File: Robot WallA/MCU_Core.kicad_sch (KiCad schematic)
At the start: 4 parts, among them IC2 STM32F407IGT6, Y1 Crystal_GND24

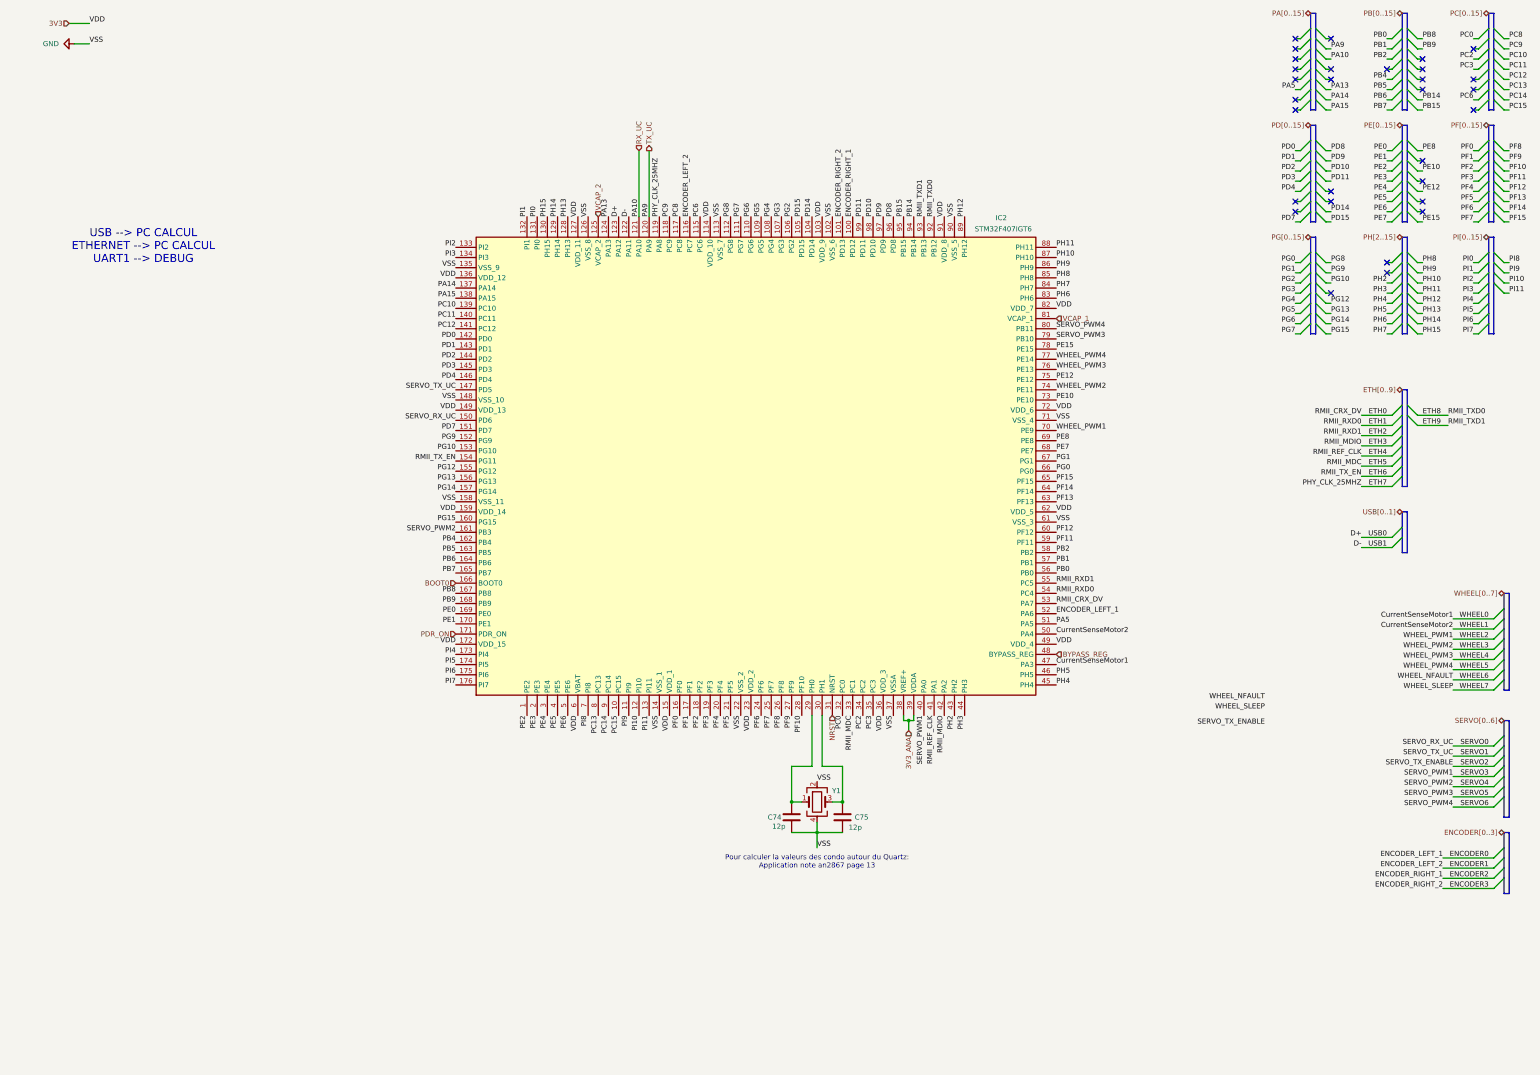
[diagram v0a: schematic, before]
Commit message: Continued to link MCU pins, Added a sheet for servomotors and optional 2 DC motors.
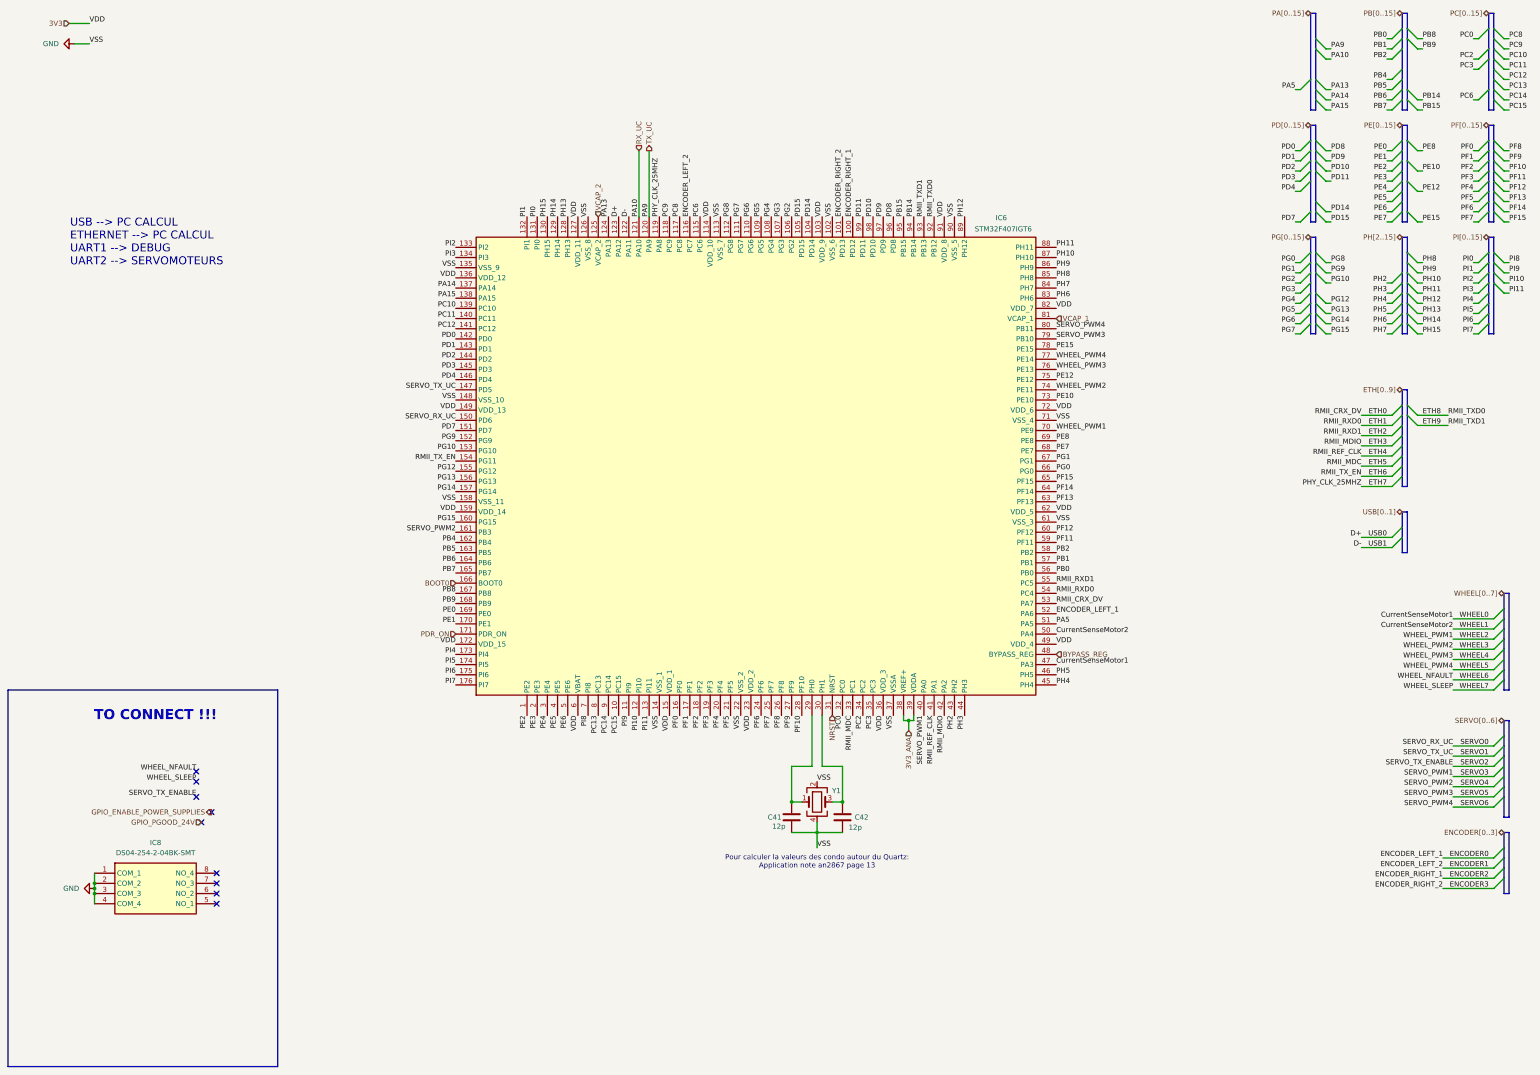
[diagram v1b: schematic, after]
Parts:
- added IC8: DS04-254-2-04BK-SMT, SOP254P990X430-8N, symbol SamacSys_new:DS04-254-2-04BK-SMT
- renumbered C74 to C41, C75 to C42, IC2 to IC6
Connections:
- net GND: now also IC8.1 (COM_1), IC8.2 (COM_2), IC8.3 (COM_3), IC8.4 (COM_4)
- no-connect marks 30 -> 9
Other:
- note added: "TO CONNECT !!!"
- note added: "USB --> PC CALCUL ETHERNET --> PC CALCUL UART1 --> DEBUG UART2 --> SERVOMOTEURS"
- note removed: "USB --> PC CALCUL ETHERNET --> PC CALCUL UART1 --> DEBUG"

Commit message: Defined every footprints
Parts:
- added J1: NC-Conn_02x05_Female, Connector_PinHeader_1.27mm:PinHeader_2x05_P1.27mm_Vertical, symbol SamacSys_Parts:Conn_02x05_Female
- C1: renamed from C41; value 12p -> 12pF; Manufacturer_Part_Number (none) -> C0603C120F5GACTU
- C2: renamed from C42; value 12p -> 12pF; Manufacturer_Part_Number (none) -> C0603C120F5GACTU
- IC1: renamed from IC6; footprint QFP50P2600X2600X160-176N -> SamacSys_Parts:QFP50P2600X2600X160-176N; Arrow Part Number STM32F407IGT6 -> (none); Arrow Price/Stock https://www.arrow.com/en/products/stm32f407igt6/stmicroelec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 -> (none); Height 1.6 -> (none); Manufacturer_Name STMicroelectronics -> (none); Mouser Part Number 511-STM32F407IGT6 -> (none); Mouser Price/Stock https://www.mouser.co.uk/ProductDetail/STMicroelectronics/S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 -> (none)
- IC2: renamed from IC8; footprint SOP254P990X430-8N -> SamacSys_Parts:SOP254P990X430-8N; Arrow Part Number DS04-254-2-04BK-SMT -> (none); Arrow Price/Stock https://www.arrow.com/en/products/ds04-254-2-04bk-smt/cui-d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 -> (none); Height 4.3 -> (none); Manufacturer_Name Same Sky -> (none); Mouser Part Number 490-DS04254204BK-SMT -> (none); Mouser Price/Stock https://www.mouser.co.uk/ProductDetail/Same-Sky/DS04-254-2-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 -> (none)
- Y1: footprint (none) -> Crystal:Crystal_SMD_3225-4Pin_3.2x2.5mm
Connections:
- net PC6 is gone; now on net ENCODER0: IC1.115 (PC6)
- net 3V3: now also J1.1
- net ENCODER0: no longer IC1.52 (PA6)
- net GND: now also J1.3, J1.5
- net NRST: now also J1.10
- net PA13 renamed SWDIO
- net SWDIO: now also J1.2
- net PA14 renamed SWCLK
- net SWCLK: now also J1.4
- net PB0 renamed SECONDARY_MOTOR1
- net PH10 renamed SECONDARY_MOTOR6
- net PH11 renamed SECONDARY_MOTOR7
- new net SECONDARY_MOTOR0: IC1.52 (PA6)
- no-connect marks 9 -> 17

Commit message: Updated USB UART converter, Linked telemeter sensors.
Updated components indicators
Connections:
- net PB4 is gone; now on net ENCODER0: IC1.162 (PB4)
- net PB5 is gone; now on net ENCODER1: IC1.163 (PB5)
- net ENCODER0: no longer IC1.115 (PC6)
- net ENCODER1: no longer IC1.116 (PC7)
- net PB1 renamed SENSORS0
- net PC0 renamed SENSORS1
- net PC2 renamed SENSORS2
- net PC3 renamed SENSORS3
- net PC8 renamed SENSORS9
- net PC9 renamed SENSORS8
- new net SENSORS10: IC1.116 (PC7)
- new net SENSORS11: IC1.115 (PC6)
- no-connect marks 17 -> 4

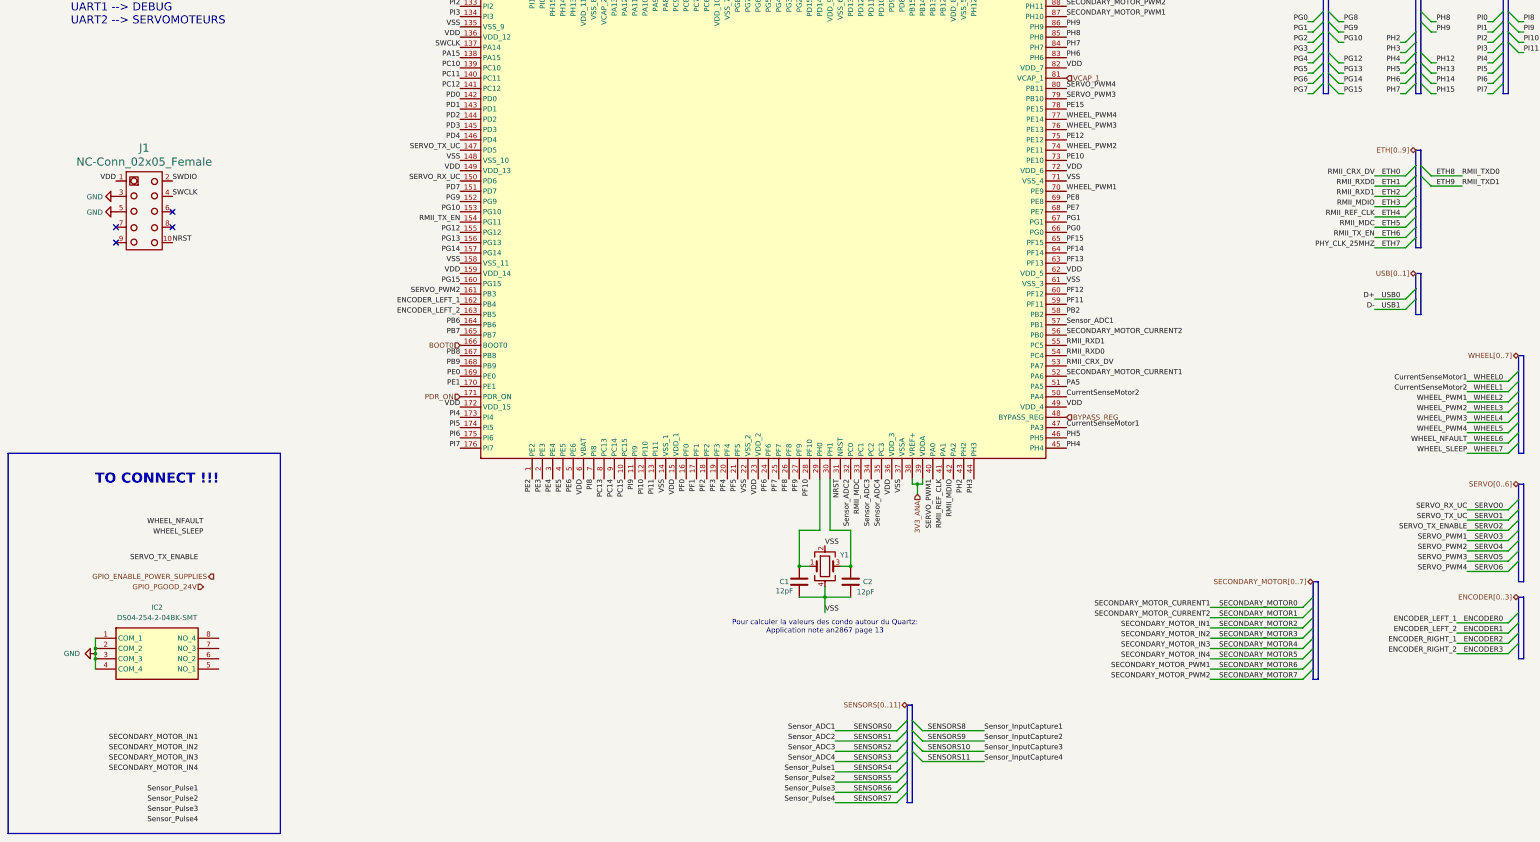
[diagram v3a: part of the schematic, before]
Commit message: Added standard switchs, debug leds and 12V and 5V connectors
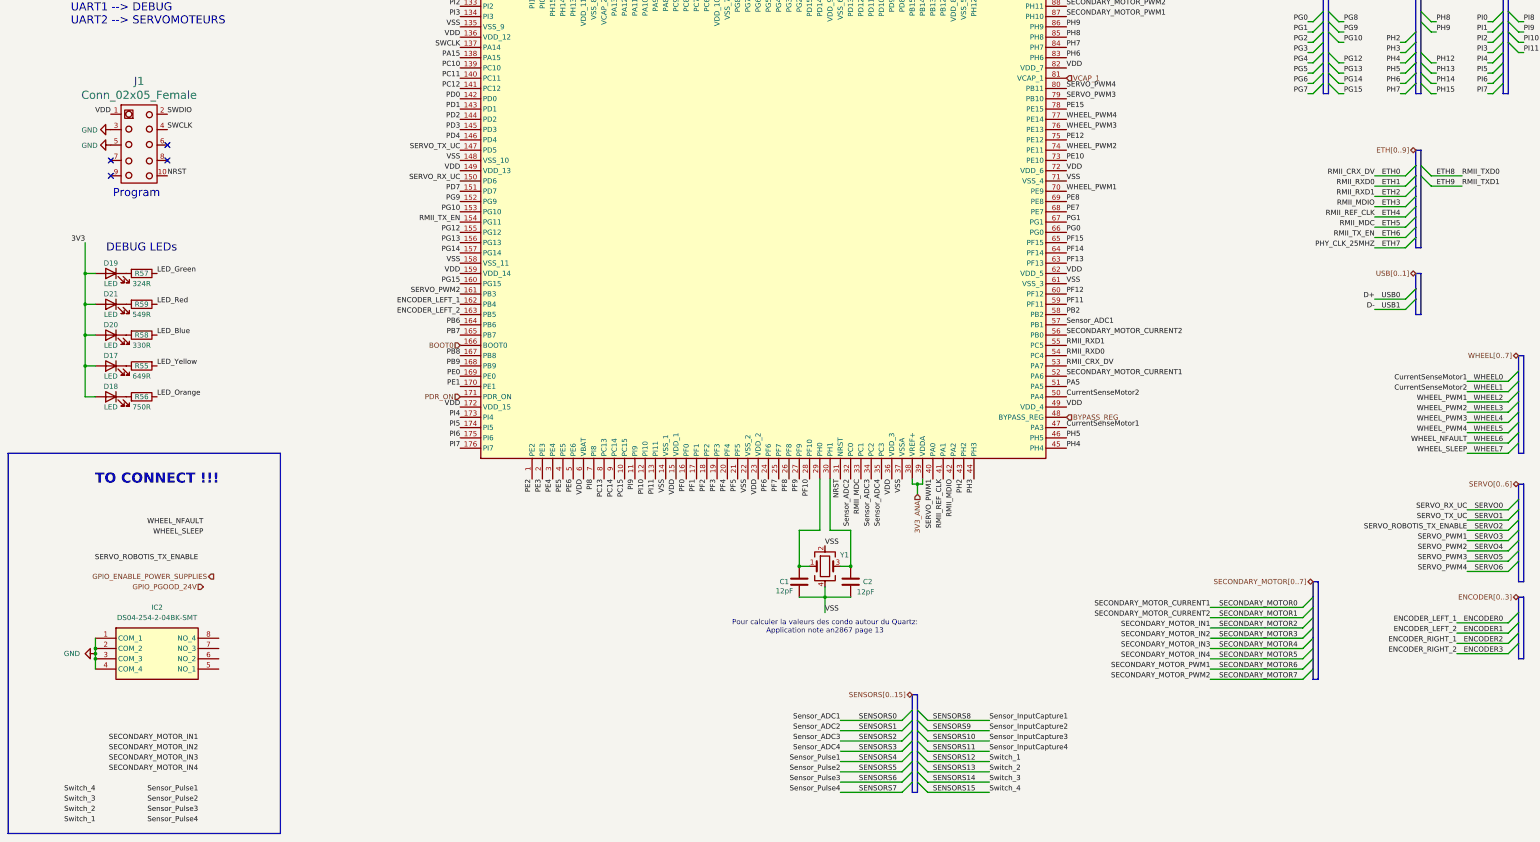
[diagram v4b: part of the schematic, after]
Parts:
- added D17, D18, D19, D20, D21: LED, LED_SMD:LED_0603_1608Metric, symbol Device:LED
- added R55: 649R, Resistor_SMD:R_0603_1608Metric, symbol Device:R
- added R56: 750R, Resistor_SMD:R_0603_1608Metric, symbol Device:R
- added R57: 324R, Resistor_SMD:R_0603_1608Metric, symbol Device:R
- added R58: 330R, Resistor_SMD:R_0603_1608Metric, symbol Device:R
- added R59: 549R, Resistor_SMD:R_0603_1608Metric, symbol Device:R
- J1: value NC-Conn_02x05_Female -> Conn_02x05_Female
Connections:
- net 3V3: now also D17.2 (A), D18.2 (A), D19.2 (A), D20.2 (A), D21.2 (A)
- new net: D17.1 (K), R55.1
- new net: D20.1 (K), R58.2
- new net: D18.1 (K), R56.2
- new net: D21.1 (K), R59.2
- new net: D19.1 (K), R57.2
- new net LED_Blue: R58.1
- new net LED_Green: R57.1
- new net LED_Orange: R56.1
- new net LED_Red: R59.1
- new net LED_Yellow: R55.2
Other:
- note added: "DEBUG LEDs"
- note added: "Program"
- moved on the sheet: J1

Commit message: Conitnue routing
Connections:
- net PA5 is gone; now on net SERVO3: IC1.51 (PA5)
- net PB14 is gone; now on net GPIO_PGOOD_24V: IC1.94 (PB14)
- net PB15 is gone; now on net GPIO_ENABLE_POWER_SUPPLIES: IC1.95 (PB15)
- net PB2 is gone; now on net SENSORS15: IC1.58 (PB2)
- net PF1 is gone; now on net WHEEL7: IC1.17 (PF1)
- net PF11 is gone; now on net SENSORS14: IC1.59 (PF11)
- net PF12 is gone; now on net SENSORS13: IC1.60 (PF12)
- net PF13 is gone; now on net SENSORS12: IC1.63 (PF13)
- net PF14 is gone; now on net SENSORS7: IC1.64 (PF14)
- net PF15 is gone; now on net SENSORS6: IC1.65 (PF15)
- net PF2 is gone; now on net WHEEL6: IC1.18 (PF2)
- net PG0 is gone; now on net SENSORS5: IC1.66 (PG0)
- net PG1 is gone; now on net SENSORS4: IC1.67 (PG1)
- net PG3 is gone; now on net SECONDARY_MOTOR2: IC1.107 (PG3)
- net PG4 is gone; now on net SECONDARY_MOTOR3: IC1.108 (PG4)
- net PG5 is gone; now on net SECONDARY_MOTOR4: IC1.109 (PG5)
- net PG6 is gone; now on net SECONDARY_MOTOR5: IC1.110 (PG6)
- net PI7 is gone; now on net SERVO2: IC1.176 (PI7)
- net ENCODER0: now also IC1.115 (PC6); no longer IC1.162 (PB4)
- net ENCODER1: now also IC1.116 (PC7); no longer IC1.163 (PB5)
- net SENSORS10: now also IC1.117 (PC8); no longer IC1.116 (PC7)
- net SENSORS11: now also IC1.118 (PC9); no longer IC1.115 (PC6)
- net SENSORS8: now also IC1.162 (PB4); no longer IC1.118 (PC9)
- net SENSORS9: now also IC1.163 (PB5); no longer IC1.117 (PC8)
- net SERVO3: no longer IC1.40 (PA0)
- new net PA0: IC1.40 (PA0)
